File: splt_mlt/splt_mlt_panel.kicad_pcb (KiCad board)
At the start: 2 copper layers, 26 x 110 mm, 53 parts, among them J1 AudioJack3_SwitchT, J10 AudioJack3_SwitchT, J11 AudioJack3_SwitchT, J12 AudioJack3_SwitchT, J13 AudioJack3_SwitchT, J14 AudioJack3_SwitchT, J15 AudioJack3_SwitchT, J16 AudioJack3_SwitchT, J17 AudioJack3_SwitchT, J2 PWR, J3 AudioJack3_SwitchT, J4 AudioJack3_SwitchT, J5 AudioJack3_SwitchT, J6 AudioJack3_SwitchT, J7 AudioJack3_SwitchT, J8 AudioJack3_SwitchT, J9 AudioJack3_SwitchT, U1 TL074, U2 TL074

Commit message: pltmlt gerbers
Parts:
- moved C8 16.1 mm to (116.8, 121.6)
- moved R13 16.1 mm to (105.3, 128.6)
- moved C3 16.1 mm to (118.8, 59.7)
- moved C9 16.1 mm to (118.8, 115.2)
- moved D2 16.1 mm to (122.3, 92.5)
- moved J1 16.1 mm to (104.1, 44.8)
- moved J12 16.1 mm to (104.1, 72.8)
- moved J13 16.1 mm to (104.1, 86.8)
- moved J16 16.1 mm to (104.1, 58.8)
- moved J17 16.1 mm to (104.1, 114.8)
- moved J2 16.1 mm to (111.1, 93.8)
- moved J3 16.1 mm to (118.1, 44.8)
- moved J4 16.1 mm to (118.1, 58.8)
- moved J5 16.1 mm to (118.1, 72.8)
- moved J6 16.1 mm to (118.1, 86.8)
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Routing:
- net (no net): vias 0 -> 18
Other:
- board size 26 x 110 mm -> 87.9 x 128.5 mm

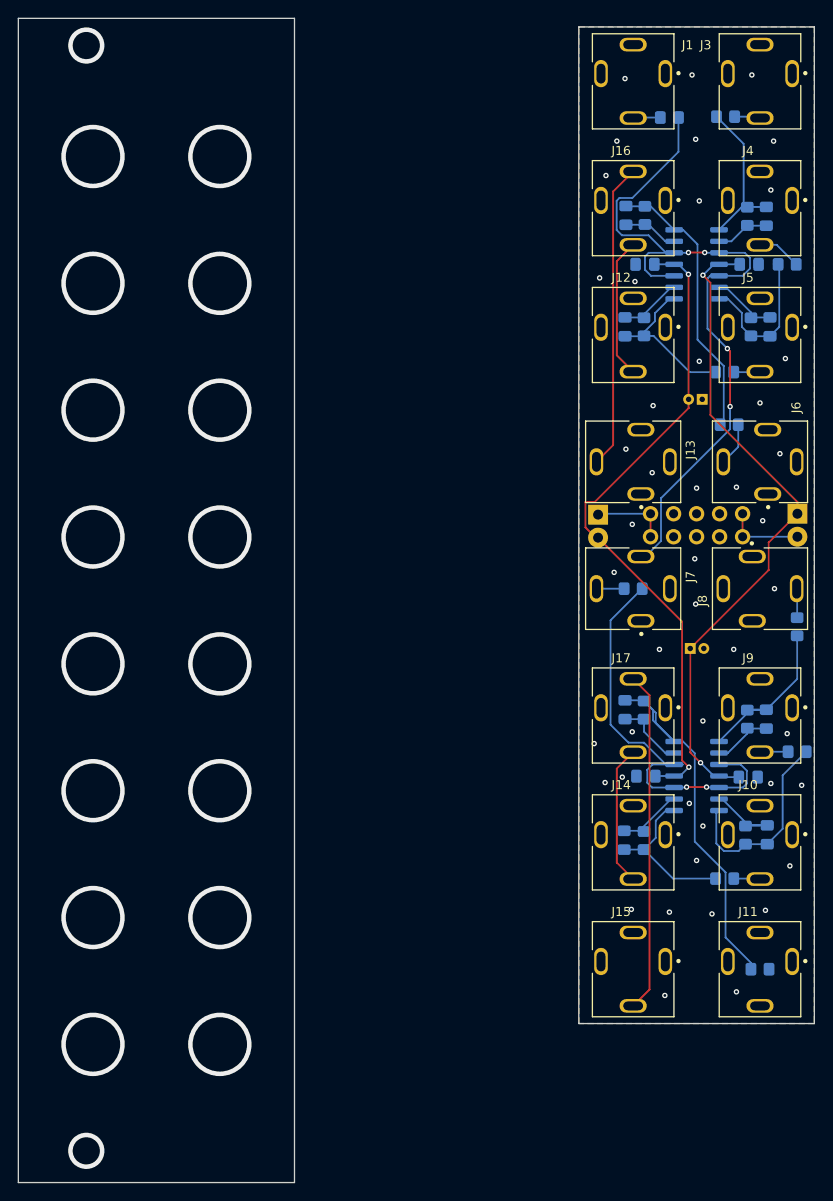
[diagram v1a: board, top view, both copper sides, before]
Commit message: Fixed some issues on the vca panner and added teletype beginnings
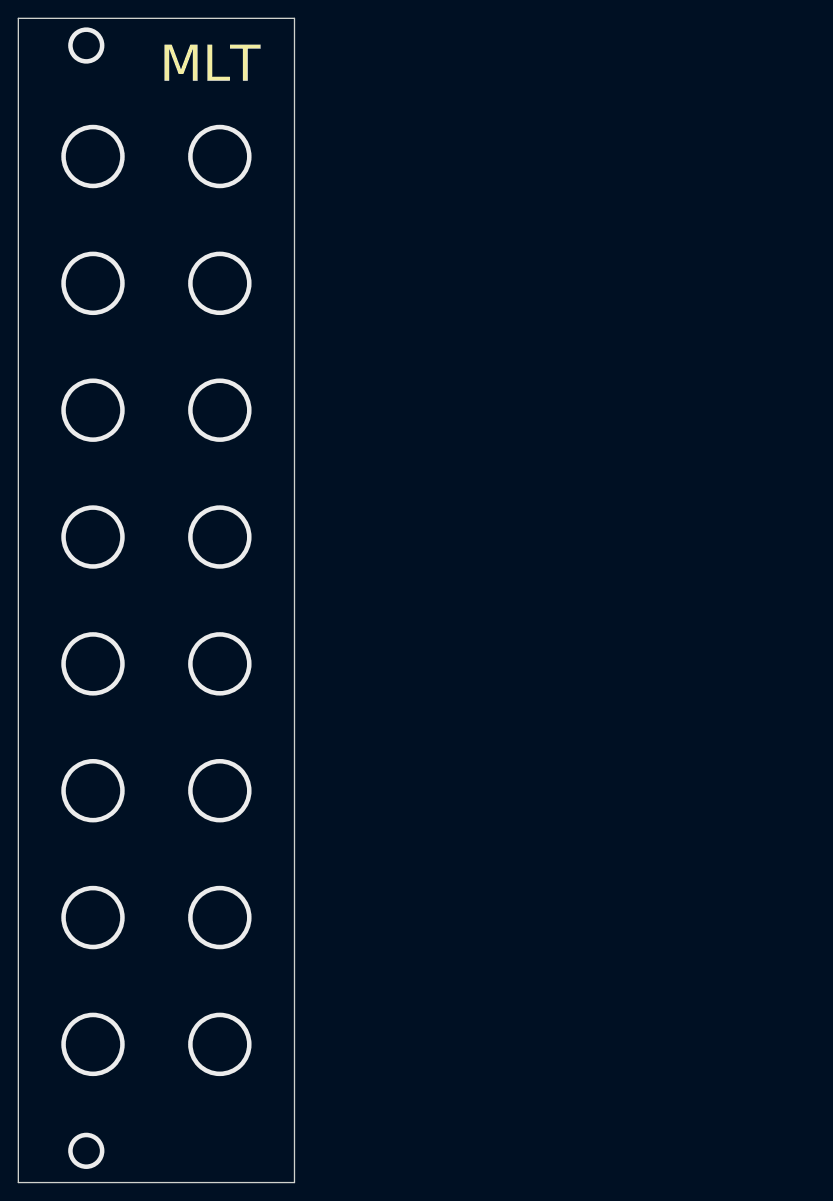
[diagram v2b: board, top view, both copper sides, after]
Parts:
- removed C1, C2, C7, C8: 100n, Capacitor_SMD:C_0805_2012Metric_Pad1.18x1.45mm_HandSolder
- removed C10, C11, C12, C3, C4, C5, C6, C9: 1n, Capacitor_SMD:C_0805_2012Metric_Pad1.18x1.45mm_HandSolder
- removed C13, C14: 10u, Capacitor_THT:CP_Radial_D4.0mm_P1.50mm
- removed D1, D2: 1N5819, Diode_THT:D_DO-41_SOD81_P2.54mm_Vertical_AnodeUp
- removed J1, J10, J11, J12, J13, J14, J15, J16, J17, J3, J4, J5, J6, J7, J8, J9: AudioJack3_SwitchT, mort_mix:CLIFF_FC681374V
- removed J2: PWR, mort_mix:Pins_2x05_2.54mm_TH_Europower_shrouded
- removed R1, R10, R11, R12, R13, R14, R15, R16, R17, R18, R2, R3, R4, R5, R6, R7, R8, R9: 0, Resistor_SMD:R_0805_2012Metric_Pad1.20x1.40mm_HandSolder
- removed U1, U2: TL074, Package_SO:SO-14_3.9x8.65mm_P1.27mm
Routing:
- net Net-(U1A-+): track 83.5 -> 0.00 mm, vias 4 -> 0
- net Net-(D1-A): track 73.0 -> 0.00 mm, vias 2 -> 0
- net Net-(D2-K): track 72.9 -> 0.00 mm, vias 2 -> 0
- net Net-(U2A-+): track 47.3 -> 0.00 mm, vias 2 -> 0
- net Net-(C12-Pad2): track 43.0 -> 0.00 mm
- net Net-(J15-PadT): track 37.6 -> 0.00 mm
- net Net-(J13-PadT): track 33.7 -> 0.00 mm
- net Net-(C6-Pad2): track 30.9 -> 0.00 mm
- net Net-(C10-Pad2): track 22.0 -> 0.00 mm
- net Net-(C9-Pad2): track 18.4 -> 0.00 mm
- net Net-(C3-Pad2): track 17.7 -> 0.00 mm
- net Net-(C11-Pad2): track 17.6 -> 0.00 mm
- net Net-(C5-Pad2): track 17.2 -> 0.00 mm
- net Net-(C4-Pad2): track 16.7 -> 0.00 mm
- net Net-(J14-PadT): track 15.5 -> 0.00 mm
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- removed copper zone on B.Cu, net GND
- removed copper zone on F.Cu, net GND
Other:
- board size 87.9 x 128.5 mm -> 30.5 x 128.5 mm
- board text added: "MLT"
